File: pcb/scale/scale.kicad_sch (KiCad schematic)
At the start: 89 parts, among them J1 USB_C_Receptacle_USB2.0, J2 Conn_01x07, J3 Conn_01x04, SW1 SW_Push, SW10 SW_Push, SW11 SW_Push, SW12 SW_Push, SW13 SW_Push, SW14 SW_Push, SW15 SW_Push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

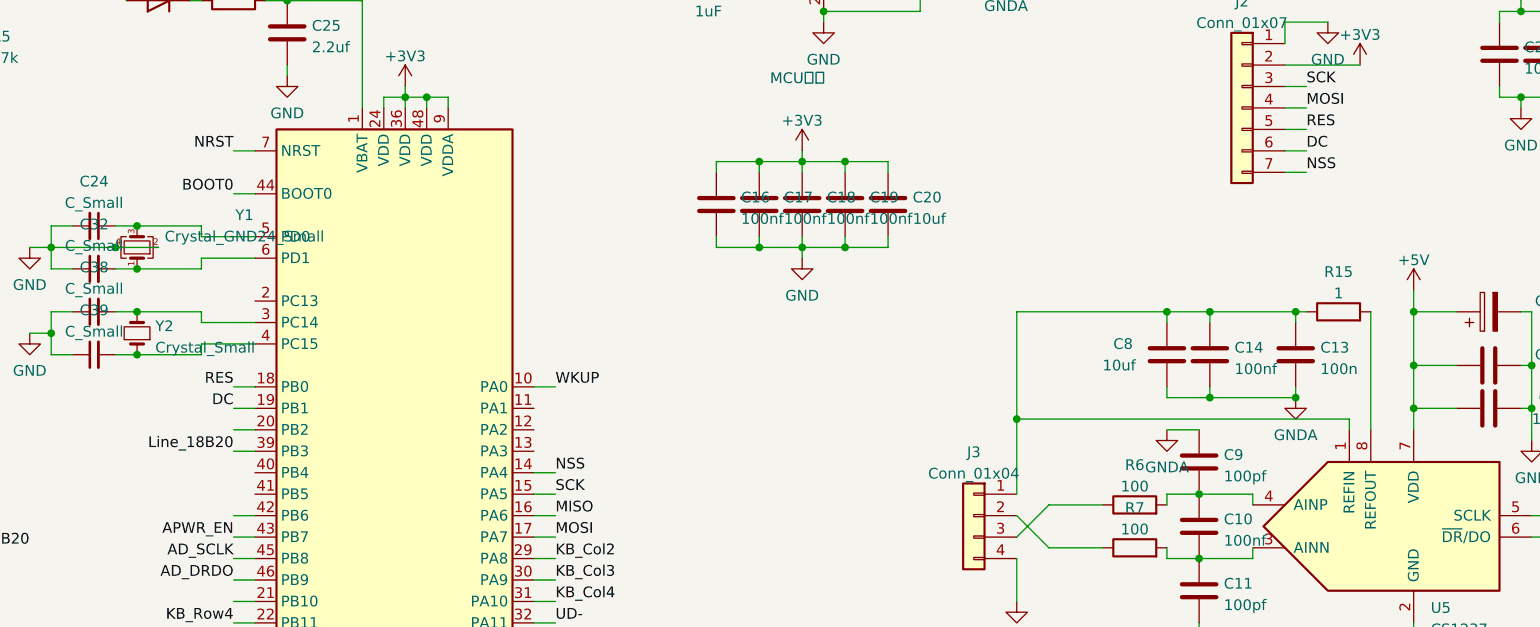
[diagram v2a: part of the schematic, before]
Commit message: OLED屏排母向下移
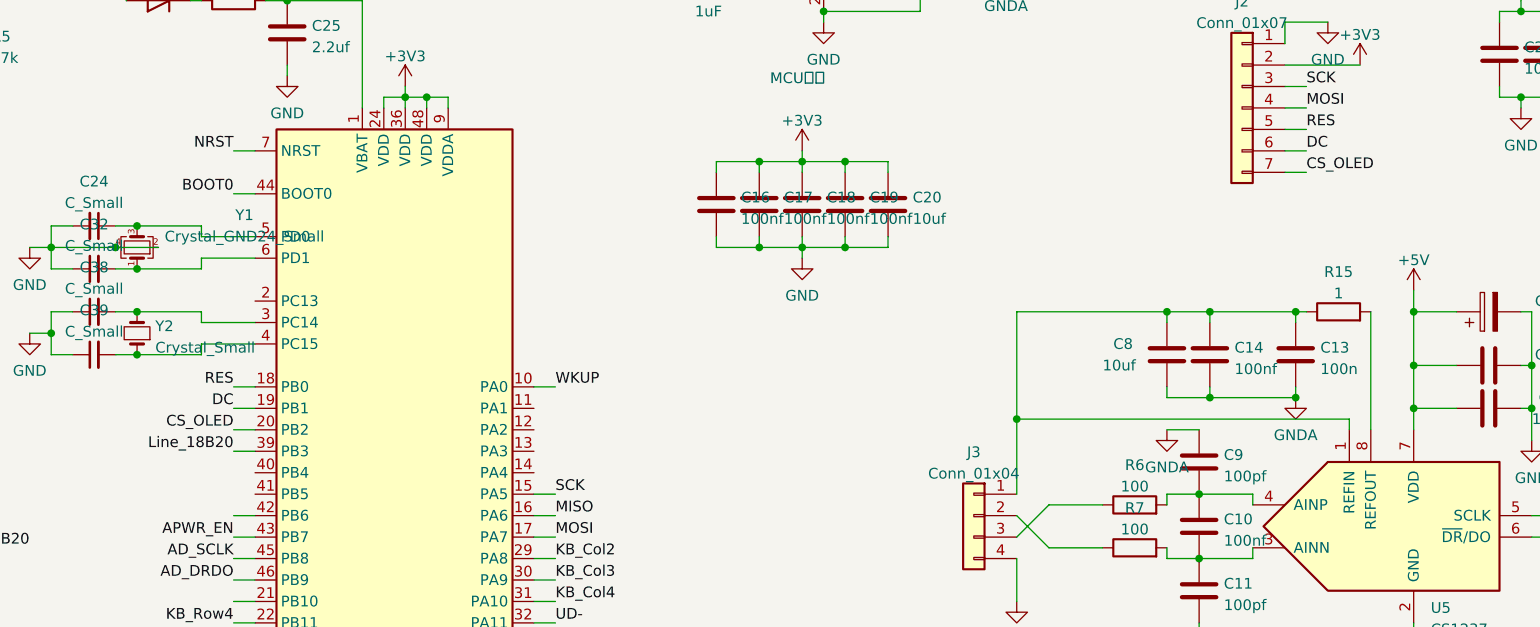
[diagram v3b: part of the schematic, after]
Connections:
- net CS_OLED: now reaches U3.20 (PB2)
- net CS_OLED: now also J2.7 (Pin_7)
- net NSS: no longer names the net of U3.14 (PA4)
- net NSS: no longer J2.7 (Pin_7)
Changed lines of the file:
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@@
-    (stroke (width 0) (type default) (color 0 0 0 0))
-  )
-  (wire (pts (xy 140.97 127) (xy 138.43 127))
     (stroke (width 0) (type default) (color 0 0 0 0))
   )
@@
     (effects (font (size 1.27 1.27)) (justify left bottom))
   )
-  (label "NSS" (at 140.97 127 0)
-    (effects (font (size 1.27 1.27)) (justify left bottom))
-  )
   (label "BOOT0" (at 72.39 71.12 180)
     (effects (font (size 1.27 1.27)) (justify right bottom))
@@
     (effects (font (size 1.27 1.27)) (justify left bottom))
   )
+  (label "CS_OLED" (at 102.87 121.92 180)
+    (effects (font (size 1.27 1.27)) (justify right bottom))
+  )
   (label "MOSI" (at 140.97 134.62 0)
     (effects (font (size 1.27 1.27)) (justify left bottom))
@@
     (effects (font (size 1.27 1.27)) (justify right bottom))
   )
-  (label "NSS" (at 229.87 91.44 0)
-    (effects (font (size 1.27 1.27)) (justify left bottom))
-  )
+  (label "CS_OLED" (at 229.87 91.44 0)
+    (effects (font (size 1.27 1.27)) (justify left bottom))
+  )

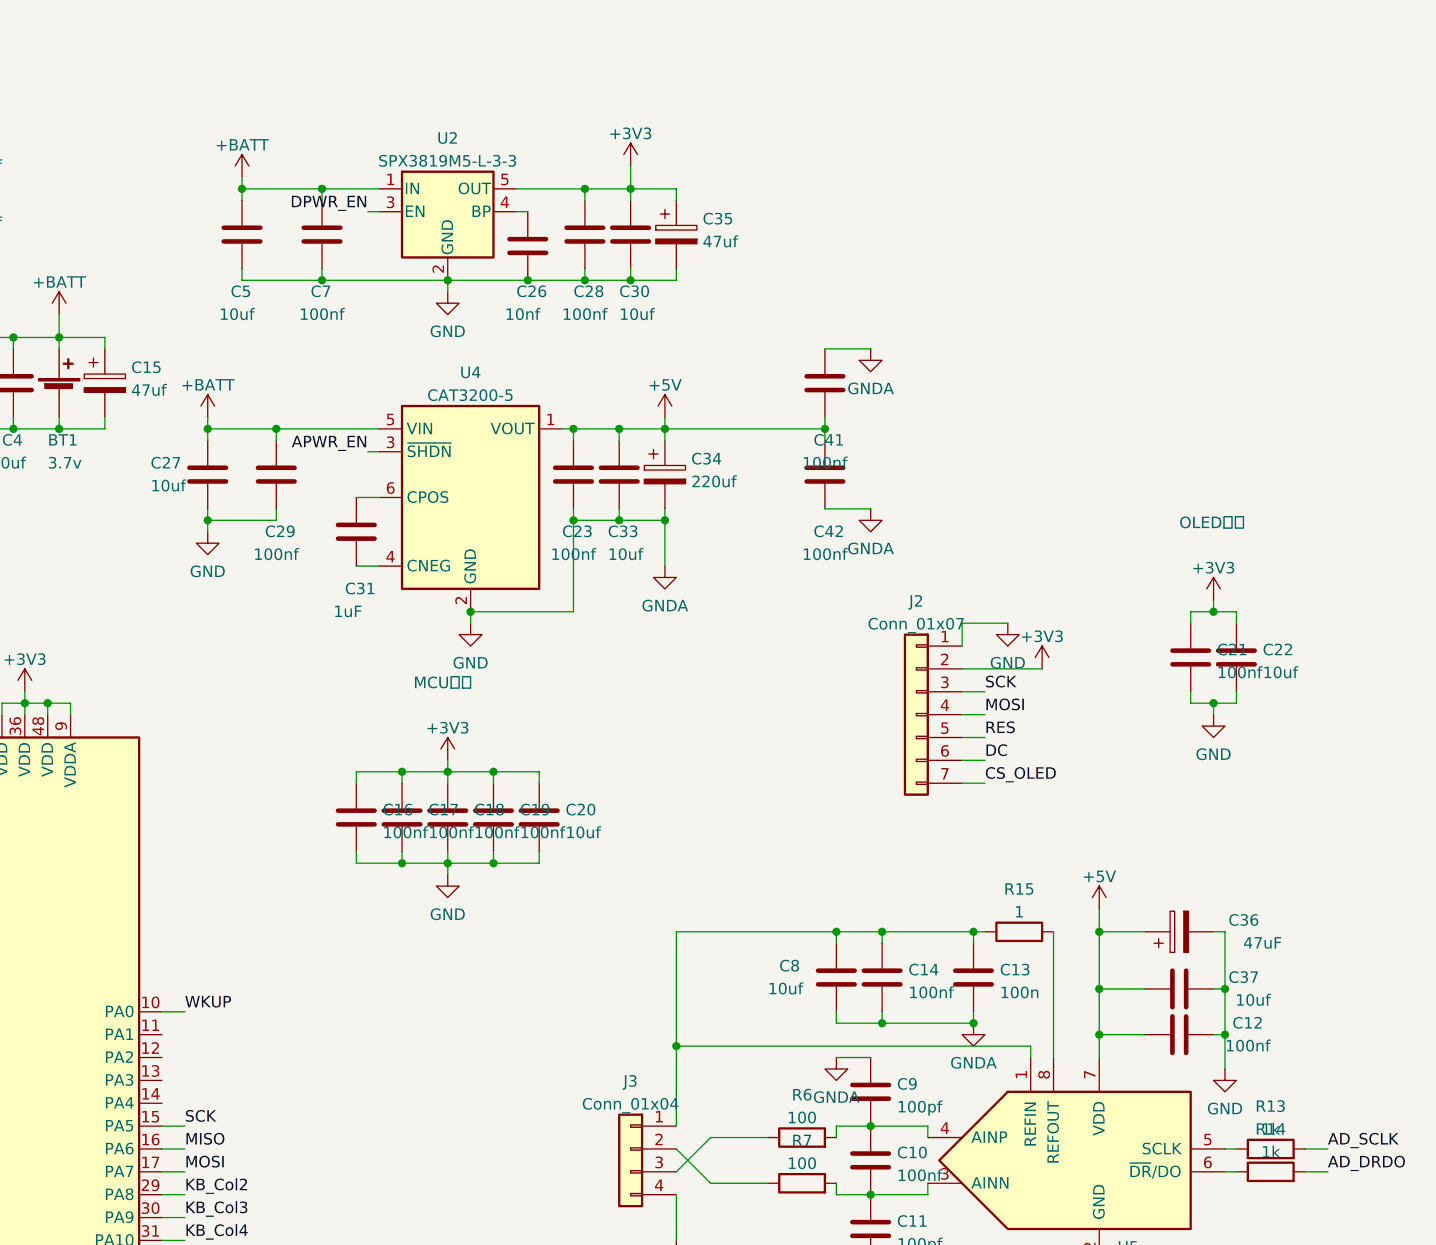
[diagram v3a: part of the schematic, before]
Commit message: 电池电压检测
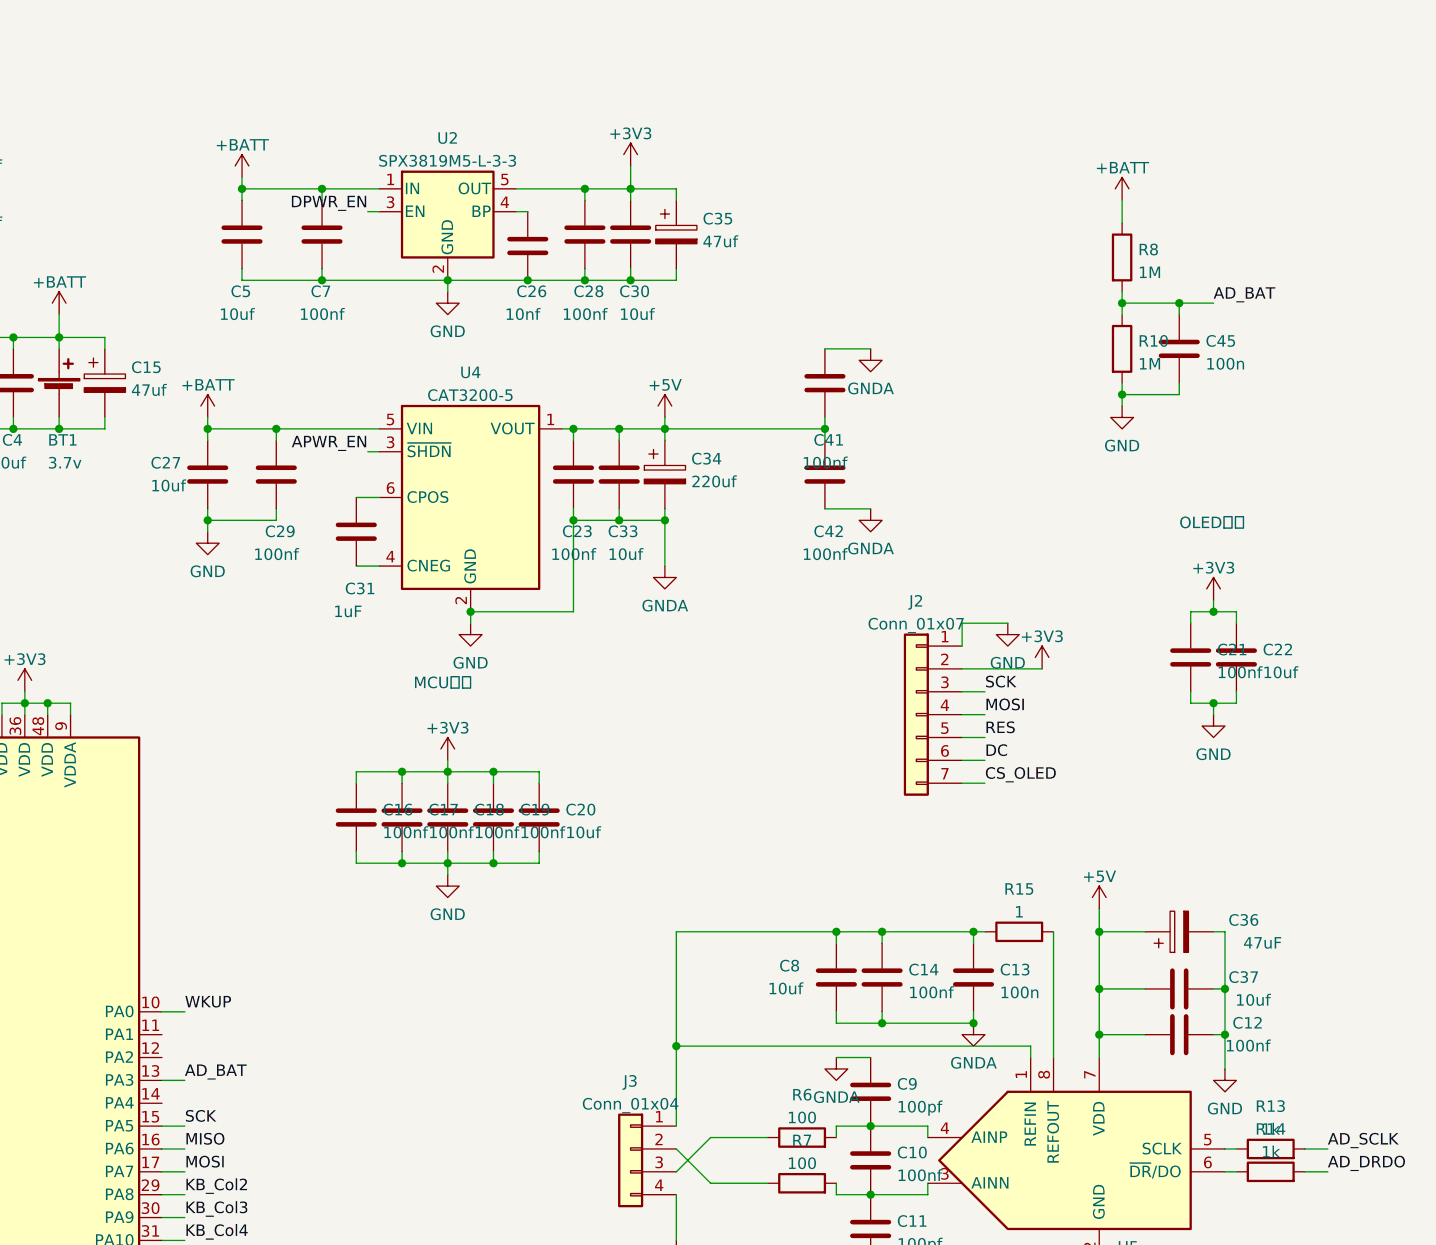
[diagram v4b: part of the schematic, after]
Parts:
- added C45: 100n, Capacitor_SMD:C_0402_1005Metric, symbol Device:C
- added R10, R8: 1M, Resistor_SMD:R_0402_1005Metric, symbol Device:R
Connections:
- net +BATT: now also R8.1
- net GND: now also C45.2, R10.2
- net AD_BAT: now reaches U3.13 (PA3)
- net AD_BAT: now also C45.1, R10.1, R8.2
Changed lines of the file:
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@@
   (junction (at 25.4 170.18) (diameter 0) (color 0 0 0 0)
   )
+  (junction (at 245.11 38.1) (diameter 0) (color 0 0 0 0)
+  )
   (junction (at 190.5 35.56) (diameter 0) (color 0 0 0 0)
   )
@@
   (junction (at 217.17 137.16) (diameter 0) (color 0 0 0 0)
   )
+  (junction (at 251.46 38.1) (diameter 0) (color 0 0 0 0)
+  )
   (junction (at 170.18 90.17) (diameter 0) (color 0 0 0 0)
   )
@@
   (junction (at 40.64 193.04) (diameter 0) (color 0 0 0 0)
   )
+  (junction (at 245.11 48.26) (diameter 0) (color 0 0 0 0)
+  )
   (junction (at 62.23 29.21) (diameter 0) (color 0 0 0 0)
   )
@@
     (stroke (width 0) (type default) (color 0 0 0 0))
   )
+  (wire (pts (xy 251.46 46.99) (xy 251.46 48.26))
+    (stroke (width 0) (type default) (color 0 0 0 0))
+  )
   (wire (pts (xy 67.31 127) (xy 67.31 125.73))
     (stroke (width 0) (type default) (color 0 0 0 0))
@@
     (stroke (width 0) (type default) (color 0 0 0 0))
   )
+  (wire (pts (xy 245.11 49.53) (xy 245.11 48.26))
+    (stroke (width 0) (type default) (color 0 0 0 0))
+  )
   (wire (pts (xy 50.8 67.31) (xy 50.8 68.58))
     (stroke (width 0) (type default) (color 0 0 0 0))
@@
     (stroke (width 0) (type default) (color 0 0 0 0))
   )
+  (wire (pts (xy 251.46 39.37) (xy 251.46 38.1))
+    (stroke (width 0) (type default) (color 0 0 0 0))
+  )
   (wire (pts (xy 48.26 105.41) (xy 49.53 105.41))
     (stroke (width 0) (type default) (color 0 0 0 0))
@@
     (stroke (width 0) (type default) (color 0 0 0 0))
   )
+  (wire (pts (xy 245.11 39.37) (xy 245.11 38.1))
+    (stroke (width 0) (type default) (color 0 0 0 0))
+  )
   (wire (pts (xy 102.87 137.16) (xy 105.41 137.16))
     (stroke (width 0) (type default) (color 0 0 0 0))
@@
     (stroke (width 0) (type default) (color 0 0 0 0))
   )
+  (wire (pts (xy 251.46 48.26) (xy 245.11 48.26))
+    (stroke (width 0) (type default) (color 0 0 0 0))
+  )
   (wire (pts (xy 227.33 73.66) (xy 232.41 73.66))
     (stroke (width 0) (type default) (color 0 0 0 0))
@@
     (stroke (width 0) (type default) (color 0 0 0 0))
   )
+  (wire (pts (xy 245.11 38.1) (xy 245.11 36.83))
+    (stroke (width 0) (type default) (color 0 0 0 0))
+  )
   (wire (pts (xy 88.9 107.95) (xy 91.44 107.95))
     (stroke (width 0) (type default) (color 0 0 0 0))
@@
     (stroke (width 0) (type default) (color 0 0 0 0))
   )
+  (wire (pts (xy 245.11 48.26) (xy 245.11 46.99))
+    (stroke (width 0) (type default) (color 0 0 0 0))
+  )
   (wire (pts (xy 212.09 50.8) (xy 212.09 52.07))
     (stroke (width 0) (type default) (color 0 0 0 0))
@@
     (stroke (width 0) (type default) (color 0 0 0 0))
   )
+  (wire (pts (xy 140.97 124.46) (xy 138.43 124.46))
+    (stroke (width 0) (type default) (color 0 0 0 0))
+  )
   (wire (pts (xy 175.26 100.33) (xy 180.34 100.33))
     (stroke (width 0) (type default) (color 0 0 0 0))
@@
     (stroke (width 0) (type default) (color 0 0 0 0))
   )
+  (wire (pts (xy 245.11 26.67) (xy 245.11 29.21))
+    (stroke (width 0) (type default) (color 0 0 0 0))
+  )
   (wire (pts (xy 50.8 191.77) (xy 52.07 191.77))
     (stroke (width 0) (type default) (color 0 0 0 0))
@@
     (stroke (width 0) (type default) (color 0 0 0 0))
   )
+  (wire (pts (xy 245.11 38.1) (xy 251.46 38.1))
+    (stroke (width 0) (type default) (color 0 0 0 0))
+  )
   (wire (pts (xy 143.51 62.23) (xy 143.51 60.96))
     (stroke (width 0) (type default) (color 0 0 0 0))
@@
     (stroke (width 0) (type default) (color 0 0 0 0))
   )
+  (wire (pts (xy 255.27 38.1) (xy 251.46 38.1))
+    (stroke (width 0) (type default) (color 0 0 0 0))
+  )
   (text "OLED电源" (at 251.46 63.5 0)
     (effects (font (size 1.27 1.27)) (justify left bottom))
@@
     (effects (font (size 1.27 1.27)) (justify left bottom))
   )
+  (label "AD_BAT" (at 255.27 38.1 0)
+    (effects (font (size 1.27 1.27)) (justify left bottom))
+  )
   (label "CS_OLED" (at 102.87 121.92 180)
     (effects (font (size 1.27 1.27)) (justify right bottom))
@@
     (effects (font (size 1.27 1.27)) (justify left bottom))
   )
+  (label "AD_BAT" (at 140.97 124.46 0)
+    (effects (font (size 1.27 1.27)) (justify left bottom))
+  )
   (label "KB_Row2" (at 22.86 177.8 180)
     (effects (font (size 1.27 1.27)) (justify right bottom))
@@
     (pin "2")
   )
+  (symbol (lib_id "Device:R") (at 245.11 43.18 0) (unit 1)
+    (in_bom yes) (on_board yes) (fields_autoplaced)
+    (property "Reference" "R10" (id 0) (at 246.888 42.3453 0)
+      (effects (font (size 1.27 1.27)) (justify left))
+    )
+    (property "Value" "1M" (id 1) (at 246.888 44.8822 0)
+      (effects (font (size 1.27 1.27)) (justify left))
+    )
+    (property "Footprint" "Resistor_SMD:R_0402_1005Metric" (id 2) (at 243.332 43.18 90)
+      (effects (font (size 1.27 1.27)) hide)
+    )
+    (property "Datasheet" "~" (id 3) (at 245.11 43.18 0)
+      (effects (font (size 1.27 1.27)) hide)
+    )
+    (pin "1")
+    (pin "2")
+  )
+  (symbol (lib_id "Device:C") (at 251.46 43.18 0) (unit 1)
+    (in_bom yes) (on_board yes) (fields_autoplaced)
+    (property "Reference" "C45" (id 0) (at 254.381 42.3453 0)
+      (effects (font (size 1.27 1.27)) (justify left))
+    )
+    (property "Value" "100n" (id 1) (at 254.381 44.8822 0)
+      (effects (font (size 1.27 1.27)) (justify left))
+    )
+    (property "Footprint" "Capacitor_SMD:C_0402_1005Metric" (id 2) (at 252.4252 46.99 0)
+      (effects (font (size 1.27 1.27)) hide)
+    )
+    (property "Datasheet" "~" (id 3) (at 251.46 43.18 0)
+      (effects (font (size 1.27 1.27)) hide)
+    )
+    (pin "1")
+    (pin "2")
+  )
   (symbol (lib_id "Device:C") (at 110.49 22.86 90) (unit 1)
     (in_bom yes) (on_board yes)
@@
     (pin "2")
   )
+  (symbol (lib_id "power:+BATT") (at 245.11 26.67 0) (unit 1)
+    (in_bom yes) (on_board yes) (fields_autoplaced)
+    (property "Reference" "#PWR022" (id 0) (at 245.11 30.48 0)
+      (effects (font (size 1.27 1.27)) hide)
+    )
+    (property "Value" "+BATT" (id 1) (at 245.11 23.0942 0))
+    (property "Footprint" "" (id 2) (at 245.11 26.67 0)
+      (effects (font (size 1.27 1.27)) hide)
+    )
+    (property "Datasheet" "" (id 3) (at 245.11 26.67 0)
+      (effects (font (size 1.27 1.27)) hide)
+    )
+    (pin "1")
+  )
   (symbol (lib_id "Device:R") (at 209.55 130.81 90) (unit 1)
     (in_bom yes) (on_board yes) (fields_autoplaced)
@@
     (pin "1")
   )
+  (symbol (lib_id "Device:R") (at 245.11 33.02 0) (unit 1)
+    (in_bom yes) (on_board yes) (fields_autoplaced)
+    (property "Reference" "R8" (id 0) (at 246.888 32.1853 0)
+      (effects (font (size 1.27 1.27)) (justify left))
+    )
+    (property "Value" "1M" (id 1) (at 246.888 34.7222 0)
+      (effects (font (size 1.27 1.27)) (justify left))
+    )
+    (property "Footprint" "Resistor_SMD:R_0402_1005Metric" (id 2) (at 243.332 33.02 90)
+      (effects (font (size 1.27 1.27)) hide)
+    )
+    (property "Datasheet" "~" (id 3) (at 245.11 33.02 0)
+      (effects (font (size 1.27 1.27)) hide)
+    )
+    (pin "1")
+    (pin "2")
+  )
   (symbol (lib_id "Device:C_Small") (at 86.36 102.87 90) (unit 1)
     (in_bom yes) (on_board yes) (fields_autoplaced)
@@
     (pin "1")
   )
+  (symbol (lib_id "power:GND") (at 245.11 49.53 0) (unit 1)
+    (in_bom yes) (on_board yes) (fields_autoplaced)
+    (property "Reference" "#PWR023" (id 0) (at 245.11 55.88 0)
+      (effects (font (size 1.27 1.27)) hide)
+    )
+    (property "Value" "GND" (id 1) (at 245.11 53.9734 0))
+    (property "Footprint" "" (id 2) (at 245.11 49.53 0)
+      (effects (font (size 1.27 1.27)) hide)
+    )
+    (property "Datasheet" "" (id 3) (at 245.11 49.53 0)
+      (effects (font (size 1.27 1.27)) hide)
+    )
+    (pin "1")
+  )
   (symbol (lib_id "power:GNDA") (at 242.57 147.32 0) (unit 1)
     (in_bom yes) (on_board yes) (fields_autoplaced)
@@
       (reference "#PWR021") (unit 1) (value "GND") (footprint "")
     )
+    (path "/8458cc08-245b-4a2f-b194-de6be2506062"
+      (reference "#PWR022") (unit 1) (value "+BATT") (footprint "")
+    )
+    (path "/f00d81c3-ab56-423d-9e39-f9971ac4e526"
+      (reference "#PWR023") (unit 1) (value "GND") (footprint "")
+    )
     (path "/6279967f-645d-46df-9144-b562915b7e91"
       (reference "#PWR028") (unit 1) (value "+BATT") (footprint "")
@@
       (reference "C43") (unit 1) (value "2.2uf") (footprint "Capacitor_SMD:C_0603_1608Metric")
     )
+    (path "/0cf80664-3e44-4213-a730-d473d5e8a122"
+      (reference "C45") (unit 1) (value "100n") (footprint "Capacitor_SMD:C_0402_1005Metric")
+    )
     (path "/527402e7-e1cd-45de-9201-4364d774830c"
       (reference "D1") (unit 1) (value "D") (footprint "Diode_SMD:D_SOD-523")
@@
       (reference "R7") (unit 1) (value "100") (footprint "Resistor_SMD:R_0402_1005Metric")
     )
+    (path "/a89cc539-8df5-4a0a-9deb-3c6441e2d80f"
+      (reference "R8") (unit 1) (value "1M") (footprint "Resistor_SMD:R_0402_1005Metric")
+    )
     (path "/274c3c7a-4cd1-4a09-97ef-4c414c00d921"
       (reference "R9") (unit 1) (value "3k") (footprint "Resistor_SMD:R_0402_1005Metric")
     )
+    (path "/0bd220eb-92f3-43e2-9a97-c9457694fb2b"
+      (reference "R10") (unit 1) (value "1M") (footprint "Resistor_SMD:R_0402_1005Metric")
+    )
     (path "/41628261-6b29-4e48-ad08-195d70dfe43a"
